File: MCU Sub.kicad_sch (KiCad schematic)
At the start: 16 parts, among them SW3 SW_Push, U6 STM32F103C8Tx, Y2 8Mhz

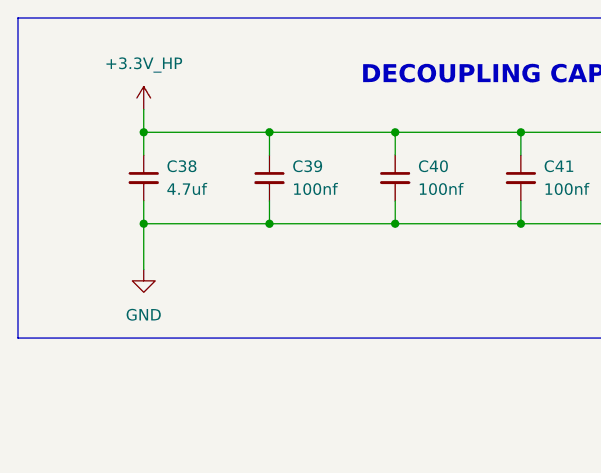
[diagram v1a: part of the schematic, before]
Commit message: [Fix] Schematic and layout. - Replaced STM32WLE5x symbol for better visualization of the symbols - Added some missing connections - Modified some components' values - Changed the layout for STM32WL
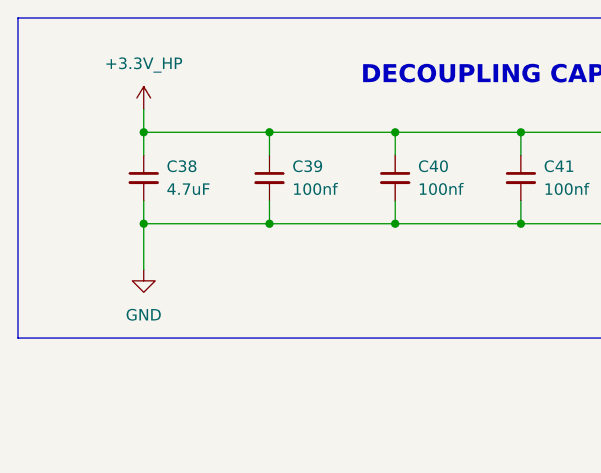
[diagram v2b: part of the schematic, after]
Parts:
- C38: value 4.7uf -> 4.7uF; footprint Capacitor_SMD:C_0402_1005Metric_Pad0.74x0.62mm_HandSolder -> Capacitor_SMD:C_0603_1608Metric
- C39, C40, C41, C42, C43, C44, C45, C46: footprint Capacitor_SMD:C_0402_1005Metric_Pad0.74x0.62mm_HandSolder -> Capacitor_SMD:C_0402_1005Metric
- R28, R29, R30: footprint Resistor_SMD:R_0402_1005Metric_Pad0.72x0.64mm_HandSolder -> Resistor_SMD:R_0402_1005Metric

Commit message: Update PCB layout
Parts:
- SW3: footprint Button_Switch_SMD:SW_Push_1P1T_NO_Vertical_Wuerth_434133025816 -> Button_Switch_SMD:SW_Tactile_SPST_NO_Straight_CK_PTS636Sx25SMTRLFS
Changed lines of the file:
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@@
 			)
 		)
-		(property "Footprint" "Button_Switch_SMD:SW_Push_1P1T_NO_Vertical_Wuerth_434133025816"
+		(property "Footprint" "Button_Switch_SMD:SW_Tactile_SPST_NO_Straight_CK_PTS636Sx25SMTRLFS"
 			(at 144.78 44.45 0)
 			(effects

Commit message: update problem
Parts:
- renumbered C38 to C42, C39 to C43, C40 to C44, C41 to C45, C42 to C46, C43 to C47, C44 to C48, C45 to C49, C46 to C50, D5 to D4, R28 to R27, R29 to R28, R30 to R29
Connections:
- net RX3: now also U6.31 (PA10); no longer U6.22 (PB11)
- net SCL1: now also U6.42 (PB6); no longer U6.45 (PB8)
- net SCL2: now also U6.21 (PB10); no longer U6.42 (PB6)
- net SDA1: now also U6.43 (PB7); no longer U6.46 (PB9)
- net SDA2: now also U6.22 (PB11); no longer U6.43 (PB7)
- net TX3: now also U6.30 (PA9); no longer U6.21 (PB10)
- no-connect marks 13 -> 11

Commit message: Update schematic
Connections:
- net +3.3V_HP renamed +3.3V
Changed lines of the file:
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@@
 			)
 		)
-		(property "Value" "+3.3V_HP"
-			(at 154.94 35.56 0)
-			(effects
-				(font
-					(size 1.27 1.27)
-				)
+		(property "Value" "+3.3V"
+			(at 157.48 39.3699 0)
+			(effects
+				(font
+					(size 1.27 1.27)
+				)
+				(justify left)
 			)
 		)
@@
 			)
 		)
-		(property "Value" "+3.3V_HP"
-			(at 187.96 53.34 0)
-			(effects
-				(font
-					(size 1.27 1.27)
-				)
+		(property "Value" "+3.3V"
+			(at 190.5 57.1499 0)
+			(effects
+				(font
+					(size 1.27 1.27)
+				)
+				(justify left)
 			)
 		)
@@
 			)
 		)
-		(property "Value" "+3.3V_HP"
-			(at 29.21 21.59 0)
-			(effects
-				(font
-					(size 1.27 1.27)
-				)
-			)
-		)
+		(property "Value" "+3.3V"
+			(at 31.75 25.3999 0)
+			(effects
+				(font
+					(size 1.27 1.27)
+				)
+				(justify left)
+			)
+		)
